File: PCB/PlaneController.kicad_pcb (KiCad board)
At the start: 2 copper layers, 44.2 x 83.8 mm, 17 parts, among them J1 Conn_01x06_Pin, J2 Conn_01x04_Pin, J3 Conn_01x03, J4 Conn_02x04_Odd_Even, J5 GPIO7, J6 GPIO8, J7 GPIO9, M1 Motor_Servo, M2 Motor_Servo, M3 Motor_Servo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

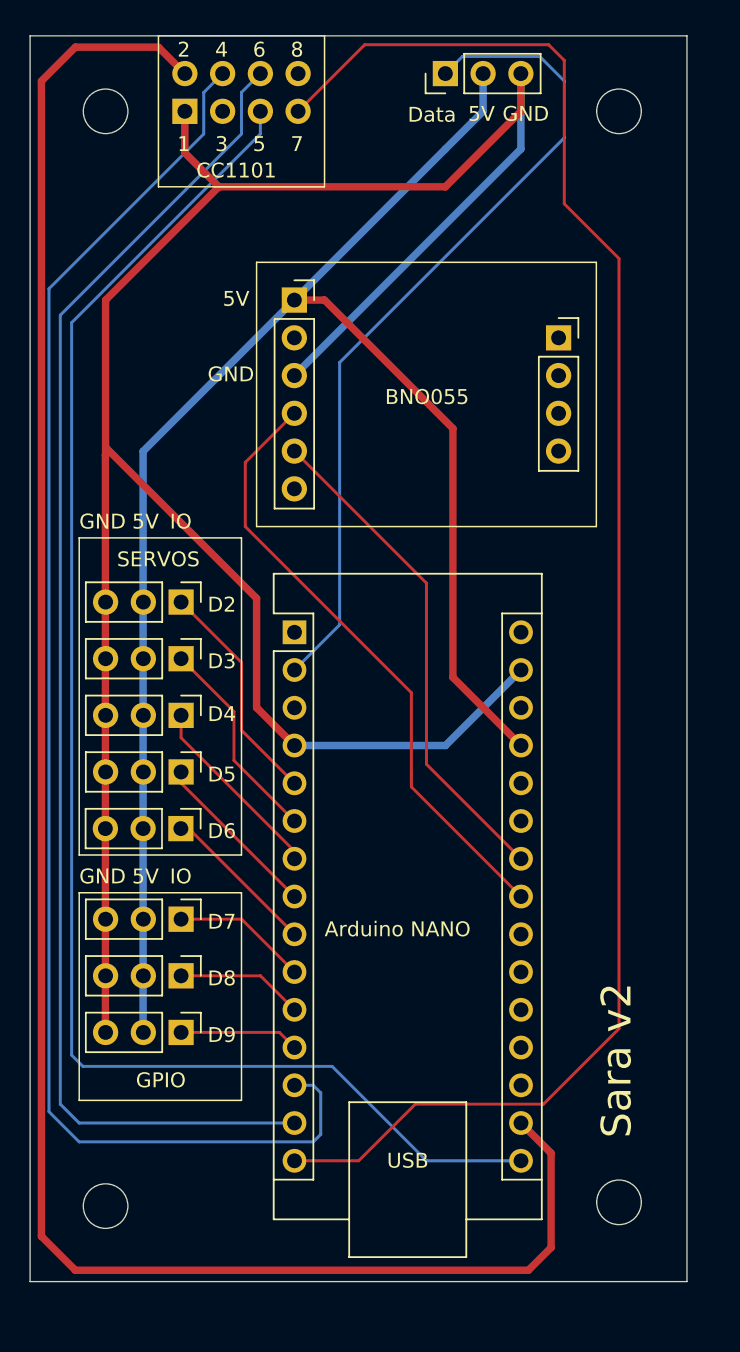
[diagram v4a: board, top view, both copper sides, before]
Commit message: Fix bug in pcb
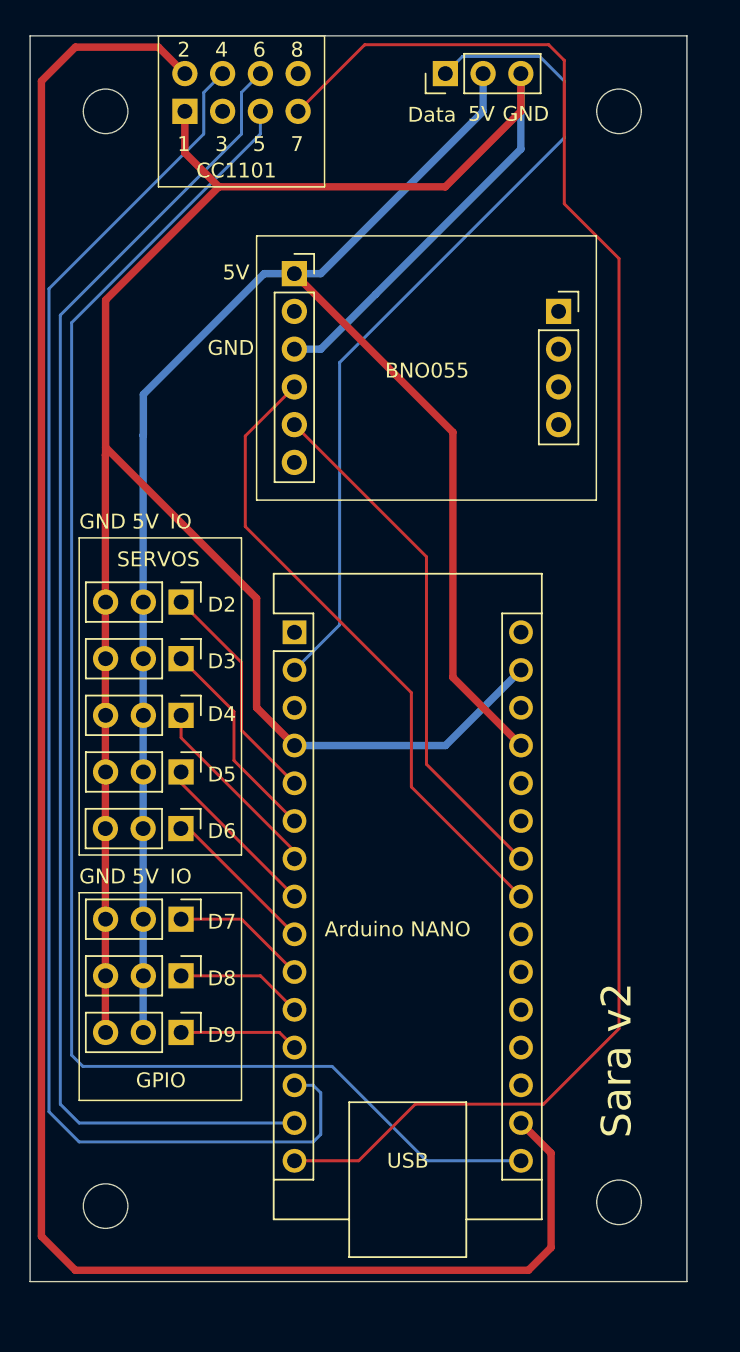
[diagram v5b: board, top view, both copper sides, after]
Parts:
- moved J1 1.78 mm to (104.1, 43.9)
- moved J2 1.78 mm to (121.9, 46.5)
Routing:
- net Net-(A1-+5V): track 111.5 -> 114.3 mm
- net Net-(A1-SDA/A4): track 41.6 -> 43.3 mm
- net Net-(A1-SCL/A5): track 33.7 -> 35.5 mm
- net /GND: track 160.4 -> 159.6 mm
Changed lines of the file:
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@@
 	(footprint "Connector_PinSocket_2.54mm:PinSocket_1x04_P2.54mm_Vertical"
 		(layer "F.Cu")
-		(at 121.92 48.26)
+		(at 121.92 46.482)
 		(descr "Through hole straight socket strip, 1x04, 2.54mm pitch, single row (from Kicad 4.0.7), script generated")
 		(tags "Through hole socket strip THT 1x04 2.54mm single row")
@@
 	(footprint "Connector_PinSocket_2.54mm:PinSocket_1x06_P2.54mm_Vertical"
 		(layer "F.Cu")
-		(at 104.14 45.72)
+		(at 104.14 43.942)
 		(descr "Through hole straight socket strip, 1x06, 2.54mm pitch, single row (from Kicad 4.0.7), script generated")
 		(tags "Through hole socket strip THT 1x06 2.54mm single row")
@@
 	)
 	(gr_rect
-		(start 101.6 43.18)
-		(end 124.46 60.96)
+		(start 101.6 41.402)
+		(end 124.46 59.182)
 		(stroke
 			(width 0.1)
@@
 	)
 	(gr_text "BNO055"
-		(at 110.236 52.832 0)
+		(at 110.236 51.054 0)
 		(layer "F.SilkS")
 		(effects
@@
 	)
 	(gr_text "GND"
-		(at 98.298 51.308 0)
+		(at 98.298 49.53 0)
 		(layer "F.SilkS")
 		(effects
@@
 	)
 	(gr_text "5V"
-		(at 99.314 46.228 0)
+		(at 99.314 44.45 0)
 		(layer "F.SilkS")
 		(effects
@@
 	)
 	(segment
-		(start 104.14 50.8)
-		(end 119.38 35.56)
+		(start 119.38 35.56)
+		(end 119.38 30.48)
 		(width 0.5)
 		(layer "B.Cu")
@@
 	)
 	(segment
-		(start 119.38 35.56)
-		(end 119.38 30.48)
+		(start 109.601 45.339)
+		(end 119.38 35.56)
 		(width 0.5)
 		(layer "B.Cu")
@@
 	)
 	(segment
-		(start 106.172 45.72)
-		(end 114.808 54.356)
+		(start 105.918 49.022)
+		(end 104.14 49.022)
 		(width 0.5)
-		(layer "F.Cu")
-		(net 7)
+		(layer "B.Cu")
+		(net 6)
 	)
 	(segment
-		(start 104.14 45.72)
-		(end 106.172 45.72)
+		(start 109.601 45.339)
+		(end 105.918 49.022)
+		(width 0.5)
+		(layer "B.Cu")
+		(net 6)
+	)
+	(segment
+		(start 104.14 43.942)
+		(end 114.808 54.61)
 		(width 0.5)
 		(layer "F.Cu")
@@
 	)
 	(segment
-		(start 114.808 54.356)
+		(start 114.808 54.61)
 		(end 114.808 71.11)
 		(width 0.5)
@@
 	)
 	(segment
-		(start 93.965 55.895)
-		(end 93.965 81.28)
+		(start 93.98 52.07)
+		(end 102.108 43.942)
 		(width 0.5)
 		(layer "B.Cu")
@@
 	)
 	(segment
-		(start 116.84 33.02)
-		(end 114.3 35.56)
+		(start 102.108 43.942)
+		(end 104.14 43.942)
 		(width 0.5)
 		(layer "B.Cu")
@@
 	)
 	(segment
-		(start 104.14 45.72)
-		(end 93.965 55.895)
+		(start 116.84 30.48)
+		(end 116.84 33.02)
+		(width 0.5)
+		(layer "B.Cu")
+		(net 7)
+	)
+	(segment
+		(start 93.98 54.803522)
+		(end 93.98 52.07)
 		(width 0.5)
 		(layer "B.Cu")
@@
 	)
 	(segment
+		(start 116.84 33.02)
+		(end 105.918 43.942)
+		(width 0.5)
+		(layer "B.Cu")
+		(net 7)
+	)
+	(segment
 		(start 93.965 94.981)
 		(end 93.98 94.996)
@@
 	)
 	(segment
-		(start 116.84 30.48)
-		(end 116.84 33.02)
+		(start 105.918 43.942)
+		(end 104.14 43.942)
 		(width 0.5)
 		(layer "B.Cu")
@@
 	)
 	(segment
-		(start 114.3 35.56)
-		(end 104.14 45.72)
+		(start 93.965 81.28)
+		(end 93.965 54.818522)
+		(width 0.5)
+		(layer "B.Cu")
+		(net 7)
+	)
+	(segment
+		(start 93.965 54.818522)
+		(end 93.98 54.803522)
 		(width 0.5)
 		(layer "B.Cu")
@@
 	)
 	(segment
-		(start 113.03 64.77)
-		(end 113.03 73.406)
-		(width 0.2)
-		(layer "F.Cu")
-		(net 11)
-	)
-	(segment
 		(start 113.03 76.952)
 		(end 119.39 83.312)
@@
 	)
 	(segment
-		(start 113.03 73.406)
+		(start 113.03 62.992)
 		(end 113.03 76.952)
 		(width 0.2)
@@
 	)
 	(segment
-		(start 104.14 55.88)
-		(end 113.03 64.77)
+		(start 104.14 54.102)
+		(end 113.03 62.992)
 		(width 0.2)
 		(layer "F.Cu")
@@
 	)
 	(segment
-		(start 112.014 78.476)
-		(end 119.39 85.852)
+		(start 100.838 54.864)
+		(end 104.14 51.562)
 		(width 0.2)
 		(layer "F.Cu")
@@
 	)
 	(segment
-		(start 112.014 77.724)
+		(start 112.014 78.476)
 		(end 112.014 72.136)
 		(width 0.2)
@@
 	)
 	(segment
-		(start 112.014 72.136)
-		(end 100.838 60.96)
-		(width 0.2)
-		(layer "F.Cu")
-		(net 23)
-	)
-	(segment
-		(start 112.014 77.724)
+		(start 119.39 85.852)
 		(end 112.014 78.476)
 		(width 0.2)
@@
 	)
 	(segment
-		(start 100.838 56.642)
-		(end 104.14 53.34)
+		(start 112.014 72.136)
+		(end 100.838 60.96)
 		(width 0.2)
 		(layer "F.Cu")
@@
 	(segment
 		(start 100.838 60.96)
-		(end 100.838 56.642)
+		(end 100.838 54.864)
 		(width 0.2)
 		(layer "F.Cu")
